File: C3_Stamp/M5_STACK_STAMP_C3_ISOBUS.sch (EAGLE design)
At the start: 3 parts, among them J1 61300811121, J2 61300611121

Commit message: ..
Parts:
- added C1, C2, C4, C5: FG18X7R1H104KNT06, FG18X7R1H104KNT06-pcb-part-libraries:FG18X7R1H104KNT06
- added C3: FG28X7R1H473KNT06, FG28X7R1H473KNT06-pcb-part-libraries:FG28X7R1H473KNT06
- added IC1: MCP2562-E_P, MCP2562-E_P-pcb-part-libraries:MCP2562-E_P
- added J3: DTF13-4P, DTF13-4P-pcb-part-libraries:DTF13-4P
- added R1, R2: (no value), resistor:R-EU_0204/7
- added U1: (no value), Wurth_Step Down Converter_MagI³C-FDSM:MAGI³C-FDSM_SIP-3_173010542_173XXXX42
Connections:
- new net +12V: C4.2, J3.1, U1.VIN
- new net +3V3: C2.2, IC1.VIO, J2.6
- new net +5V: C1.2, C5.2, IC1.VDD, J1.8, U1.VOUT
- new net CAN_N: IC1.CANL, J3.4, R2.1
- new net CAN_P: IC1.CANH, J3.2, R1.2
- new net EN: J2.3
- new net G10: J1.7
- new net G20: IC1.RXD, J2.4
- new net G21: IC1.TXD, J2.5
- new net G4: J1.2
- new net G5: J1.3
- new net G6: J1.4
- new net G7: J1.5
- new net G8: J1.6
- new net G9: J2.2
- new net GND: C1.1, C2.1, C3.2, C4.1, C5.1, IC1.STBY, IC1.VSS, J1.1, J2.1, J3.3, U1.GND
- new net N$1: C3.1, R1.1, R2.2
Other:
- moved on the sheet: J1, J2

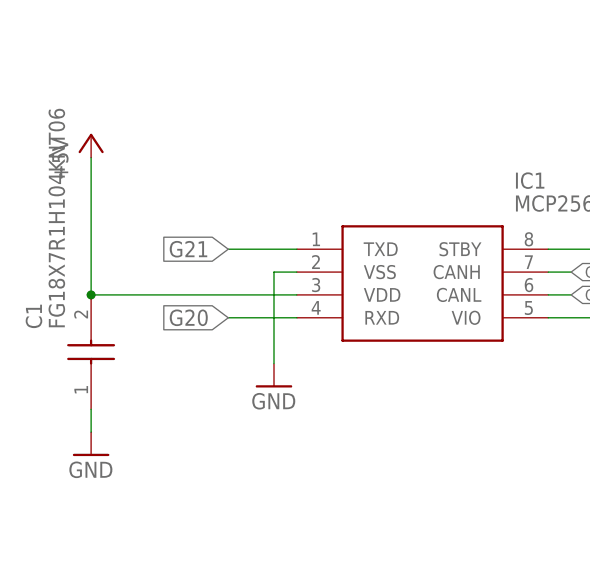
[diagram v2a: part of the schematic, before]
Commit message: was a bad bug about 2 Pins.
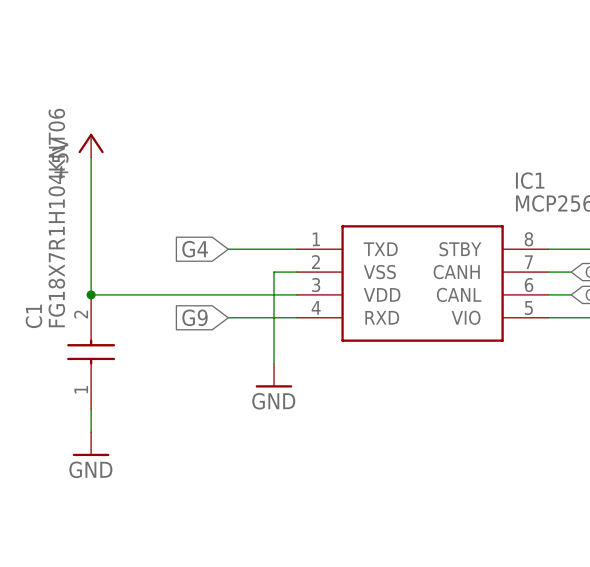
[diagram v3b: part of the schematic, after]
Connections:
- net G20: no longer IC1.RXD
- net G21: no longer IC1.TXD
- net G4: now also IC1.TXD
- net G9: now also IC1.RXD
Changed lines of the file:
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@@
 <label x="25.4" y="86.36" size="1.27" layer="95" xref="yes"/>
+</segment>
+<segment>
+<pinref part="IC1" gate="G$1" pin="RXD"/>
+<wire x1="2.54" y1="25.4" x2="-5.08" y2="25.4" width="0.1524" layer="91"/>
+<label x="-5.08" y="25.4" size="1.778" layer="95" rot="R180" xref="yes"/>
 </segment>
 </net>
@@
 <label x="-5.08" y="99.06" size="1.27" layer="95" rot="R180" xref="yes"/>
 </segment>
-</net>
-<net name="G21" class="0">
 <segment>
 <pinref part="IC1" gate="G$1" pin="TXD"/>
@@
 <label x="-5.08" y="33.02" size="1.778" layer="95" rot="R180" xref="yes"/>
 </segment>
+</net>
+<net name="G21" class="0">
 <segment>
 <pinref part="J2" gate="G$1" pin="5"/>
@@
 <net name="G20" class="0">
 <segment>
-<pinref part="IC1" gate="G$1" pin="RXD"/>
-<wire x1="2.54" y1="25.4" x2="-5.08" y2="25.4" width="0.1524" layer="91"/>
-<label x="-5.08" y="25.4" size="1.778" layer="95" rot="R180" xref="yes"/>
-</segment>
-<segment>
 <pinref part="J2" gate="G$1" pin="4"/>
